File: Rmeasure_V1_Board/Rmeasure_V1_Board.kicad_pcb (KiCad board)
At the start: 2 copper layers, 58 x 28.5 mm, 50 parts, among them J1 USB_C_Receptacle_USB2.0, J2 CON_debug, J3 Conn_ARM_JTAG_SWD_10, J4 CON_CAN, J5 CON_CAN, U1 STM32F302C6Tx, U2 NCP1117-3.3_SOT223, U3 SN65HVD232, Y1 8MHz

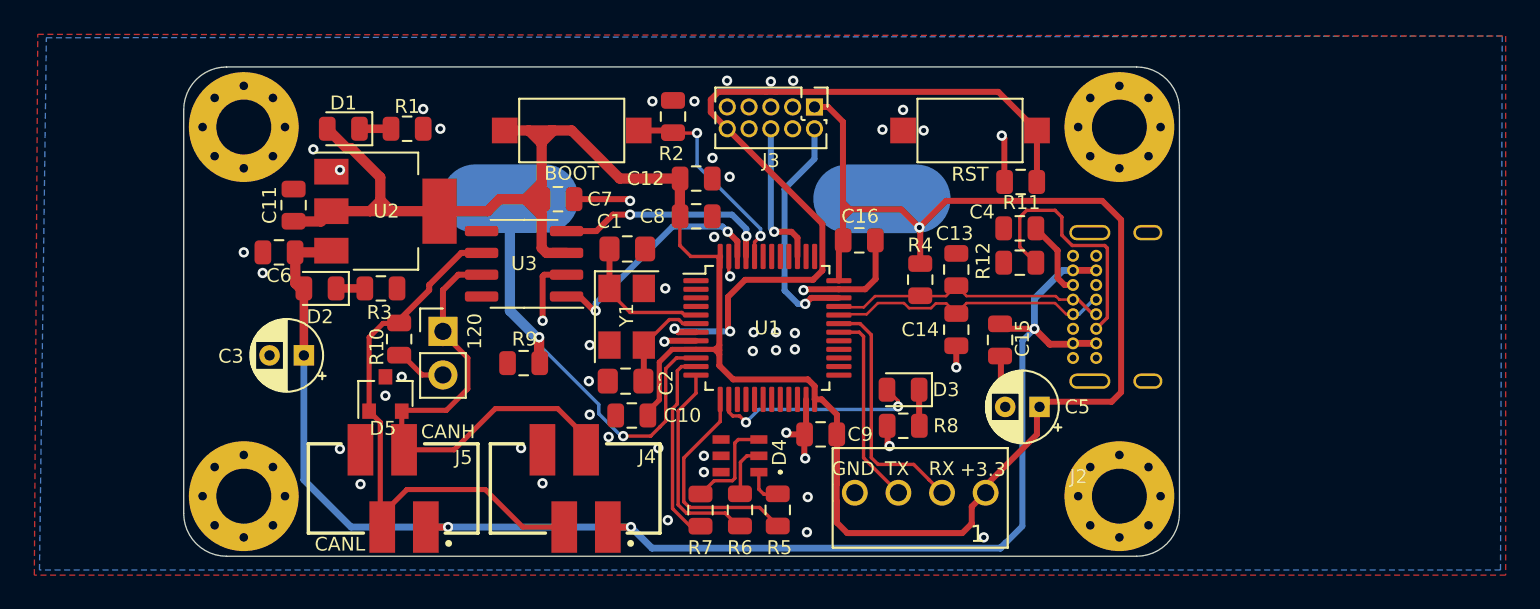
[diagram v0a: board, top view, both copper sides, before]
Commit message: IO prete, Pompe finir sérigraphie, Alim+AX12 à faire
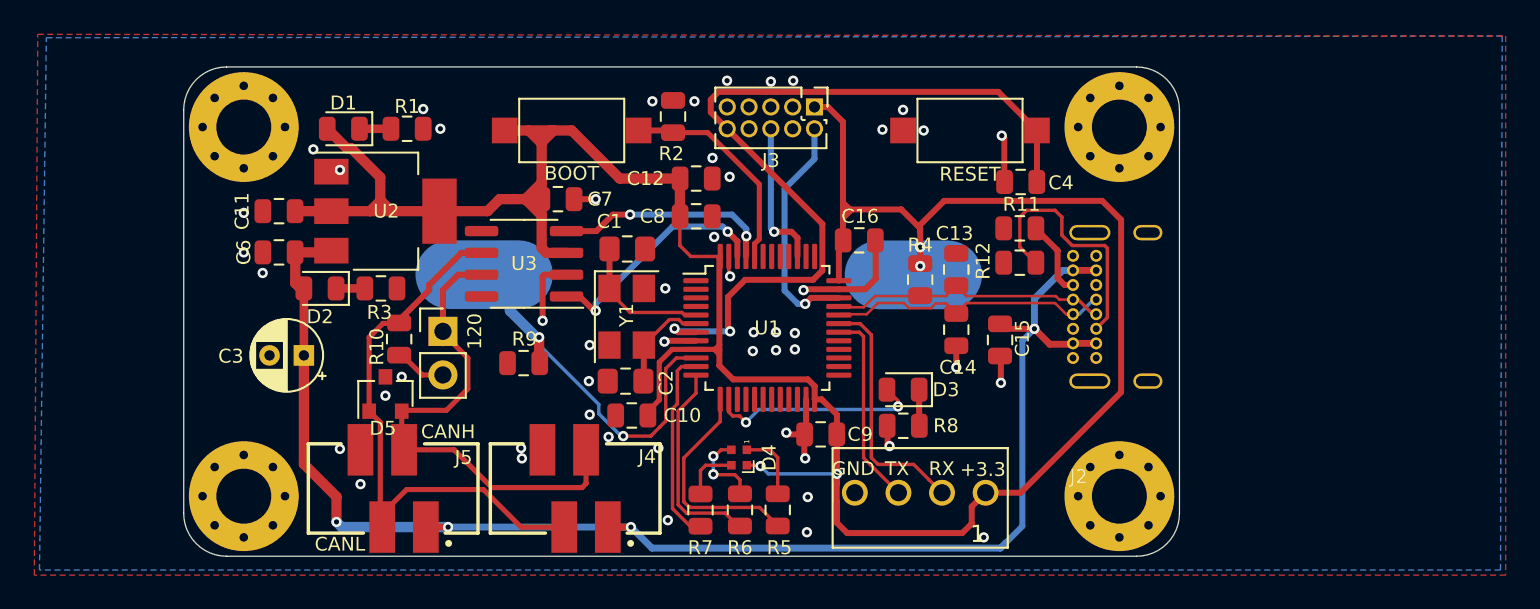
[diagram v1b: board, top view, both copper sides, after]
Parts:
- removed C5: 10u, Capacitor_THT:CP_Radial_D4.0mm_P2.00mm
- D4: value LED_RGB -> LED_RGBA; footprint AREA_lib_composant:LED_RGB_LTRBRASF6B6C011200R18 -> LED_SMD:LED_SK6812_EC15_1.5x1.5mm
- moved TP1 4.68 mm to (84.9, 90.1)
- moved C11 0.92 mm to (73.0, 86.4), turned to 180 degrees
- moved D4 0.11 mm to (99.8, 100.8), turned to 270 degrees
- renumbered RST to RESET
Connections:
- D4 pad 4: GND -> +3V3
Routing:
- net +3V3: track 147.9 -> 151.7 mm, vias 1 -> 4
- net /R_point: track 26.1 -> 23.2 mm
- net Net-(D4-Pad3): track 5.93 -> 3.30 mm
- net GND: track 29.6 -> 27.6 mm, vias 52 -> 51
- net Net-(D4-Pad1): track 2.22 -> 4.10 mm
- net Net-(D4-Pad2): track 3.10 -> 4.75 mm, vias 0 -> 2
- net /CANH: track 29.4 -> 29.9 mm
- net +5V: track 86.3 -> 86.6 mm, vias 3 -> 4
- net /BOOT0: track 12.3 -> 12.6 mm, vias 2 -> 0

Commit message: lots of stuf
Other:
- net class Default removed

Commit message: PCB RMEAS ok to fab
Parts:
- removed J3: Conn_ARM_JTAG_SWD_10, Connector_PinHeader_1.27mm:PinHeader_2x05_P1.27mm_Vertical
- moved C4 4.45 mm to (111.7, 84.5)
- moved RESET 4.45 mm to (108.8, 81.5)
- renumbered 120 to JP1
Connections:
- J1 pad A8: Net-(J1-PadA8) -> unconnected-(J1-PadA8)
- J1 pad B8: Net-(J1-PadB8) -> unconnected-(J1-PadB8)
- U1 pad 1: Net-(U1-Pad1) -> unconnected-(U1-Pad1)
- U1 pad 15: Net-(U1-Pad15) -> unconnected-(U1-Pad15)
- U1 pad 16: Net-(U1-Pad16) -> unconnected-(U1-Pad16)
- U1 pad 17: Net-(U1-Pad17) -> unconnected-(U1-Pad17)
- U1 pad 18: Net-(U1-Pad18) -> unconnected-(U1-Pad18)
- U1 pad 19: Net-(U1-Pad19) -> unconnected-(U1-Pad19)
- U1 pad 2: Net-(U1-Pad2) -> unconnected-(U1-Pad2)
- U1 pad 20: Net-(U1-Pad20) -> unconnected-(U1-Pad20)
- U1 pad 21: Net-(U1-Pad21) -> unconnected-(U1-Pad21)
- U1 pad 22: Net-(U1-Pad22) -> unconnected-(U1-Pad22)
- U1 pad 25: Net-(U1-Pad25) -> unconnected-(U1-Pad25)
- U1 pad 26: Net-(U1-Pad26) -> unconnected-(U1-Pad26)
- U1 pad 27: Net-(U1-Pad27) -> unconnected-(U1-Pad27)
- U1 pad 28: Net-(U1-Pad28) -> unconnected-(U1-Pad28)
- U1 pad 29: Net-(U1-Pad29) -> unconnected-(U1-Pad29)
- U1 pad 3: Net-(U1-Pad3) -> unconnected-(U1-Pad3)
- U1 pad 38: Net-(U1-Pad38) -> unconnected-(U1-Pad38)
- U1 pad 4: Net-(U1-Pad4) -> unconnected-(U1-Pad4)
- U1 pad 40: Net-(U1-Pad40) -> unconnected-(U1-Pad40)
- U1 pad 41: Net-(U1-Pad41) -> unconnected-(U1-Pad41)
- U1 pad 42: Net-(U1-Pad42) -> unconnected-(U1-Pad42)
- U1 pad 43: Net-(U1-Pad43) -> unconnected-(U1-Pad43)
- U3 pad 5: Net-(U3-Pad5) -> unconnected-(U3-Pad5)
- U3 pad 8: Net-(U3-Pad8) -> unconnected-(U3-Pad8)
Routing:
- net /RST: track 48.6 -> 30.4 mm
- net /SWDIO: track 13.8 -> 0.00 mm, vias 1 -> 0
- net /SWO: track 8.67 -> 0.00 mm, vias 1 -> 0
- net +3V3: track 151.7 -> 144.0 mm
- net /R_point: track 23.2 -> 17.8 mm
- net +5V: track 86.6 -> 86.0 mm
- net GND: vias 51 -> 55
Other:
- board text added: "."
